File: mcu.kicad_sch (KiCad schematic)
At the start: 34 parts, among them J2 USB-C, J3 UART0, J4 I2C / Qwiic, J5 SPI, J6 WS2812, J7 Spare IO, J8 Rail break-out, SW1 RESET, SW2 BOOT, U4 ESP32-S3-WROOM-1-N16R8, U5 USBLC6-2SC6, U6 74AHCT1G125

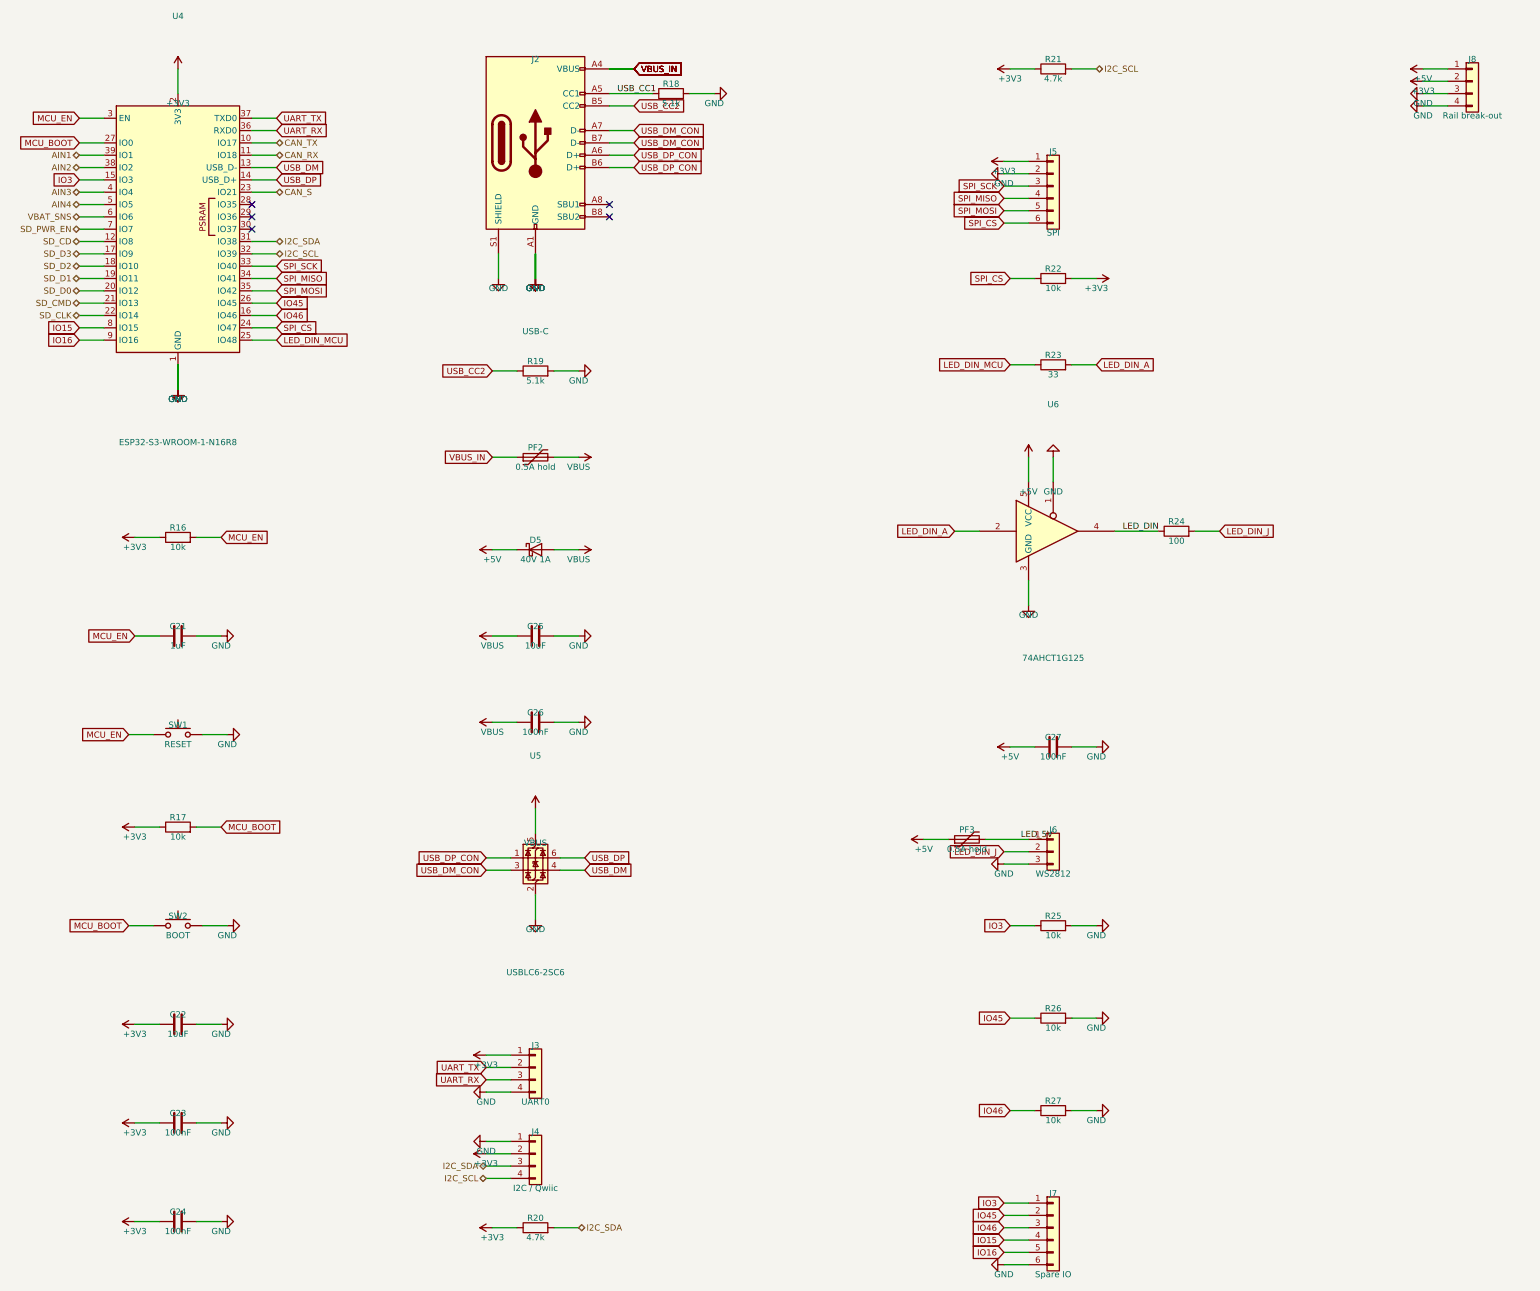
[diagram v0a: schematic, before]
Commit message: Turn the USB-C round, clamp ahead of the FET, draw the last two blocks
Two review findings from Matt, both correct:

  - The USB-C receptacle faced the wrong way. Its fab outline runs
    y -3.65..+3.65 and the signal pads sit at y -4.04, outside it: the
    contacts leave the REAR of the shell, so at 0 degrees the mouth faces
    +y, and at the 270 it was placed at the opening pointed back into the
    middle of the board. At 90 the mouth ends ~2 mm inside the right edge
    -- the plug approaches over the top of the laminate, so those last
    2 mm are not in its way -- and the pad row faces inboard, which is
    where the D+/D- via columns and the USBLC6 already were.

  - The transient clamp was behind the reverse-battery FET, which leaves
    Q1 and the LM74700 exposed to whatever arrives on the harness: on a
    negative transient Q1 turns off and stands the whole pulse across its
    drain-source, and ISO 7637-2 pulse 1 (-100V) and 3a (-150V) both
    exceed its 100V rating. It now sits on VBAT_F, straight after the
    fuse and ahead of the ferrite and the FET.

    It also changes from SMCJ40A to SMCJ40CA. A unidirectional part in
    that position forward-conducts on a sustained reverse connection and
    blows the fuse -- exactly the outcome the ideal diode exists to
    avoid. Bidirectional stands off 40V either way, so -14V reverse
    battery is still Q1's job to block and only real transients clamp.
    Needs an LCSC pick at order time, as the SMCJ40A did.

The power front end and the USB port are now hand-drawn blocks too, so
every recurring circuit on the board comes from gen/sch_blocks.py.

Board rerouted from scratch at 60 autoroute passes: 0 DRC violations,
0 unconnected. Netlist matches node for node, ERC clean. fab/ regenerated.

Co-Authored-By: Claude Opus 5 <noreply@anthropic.com>
Claude-Session: https://claude.ai/code/session_01DhNbL25h25p8VFCjRfJik9
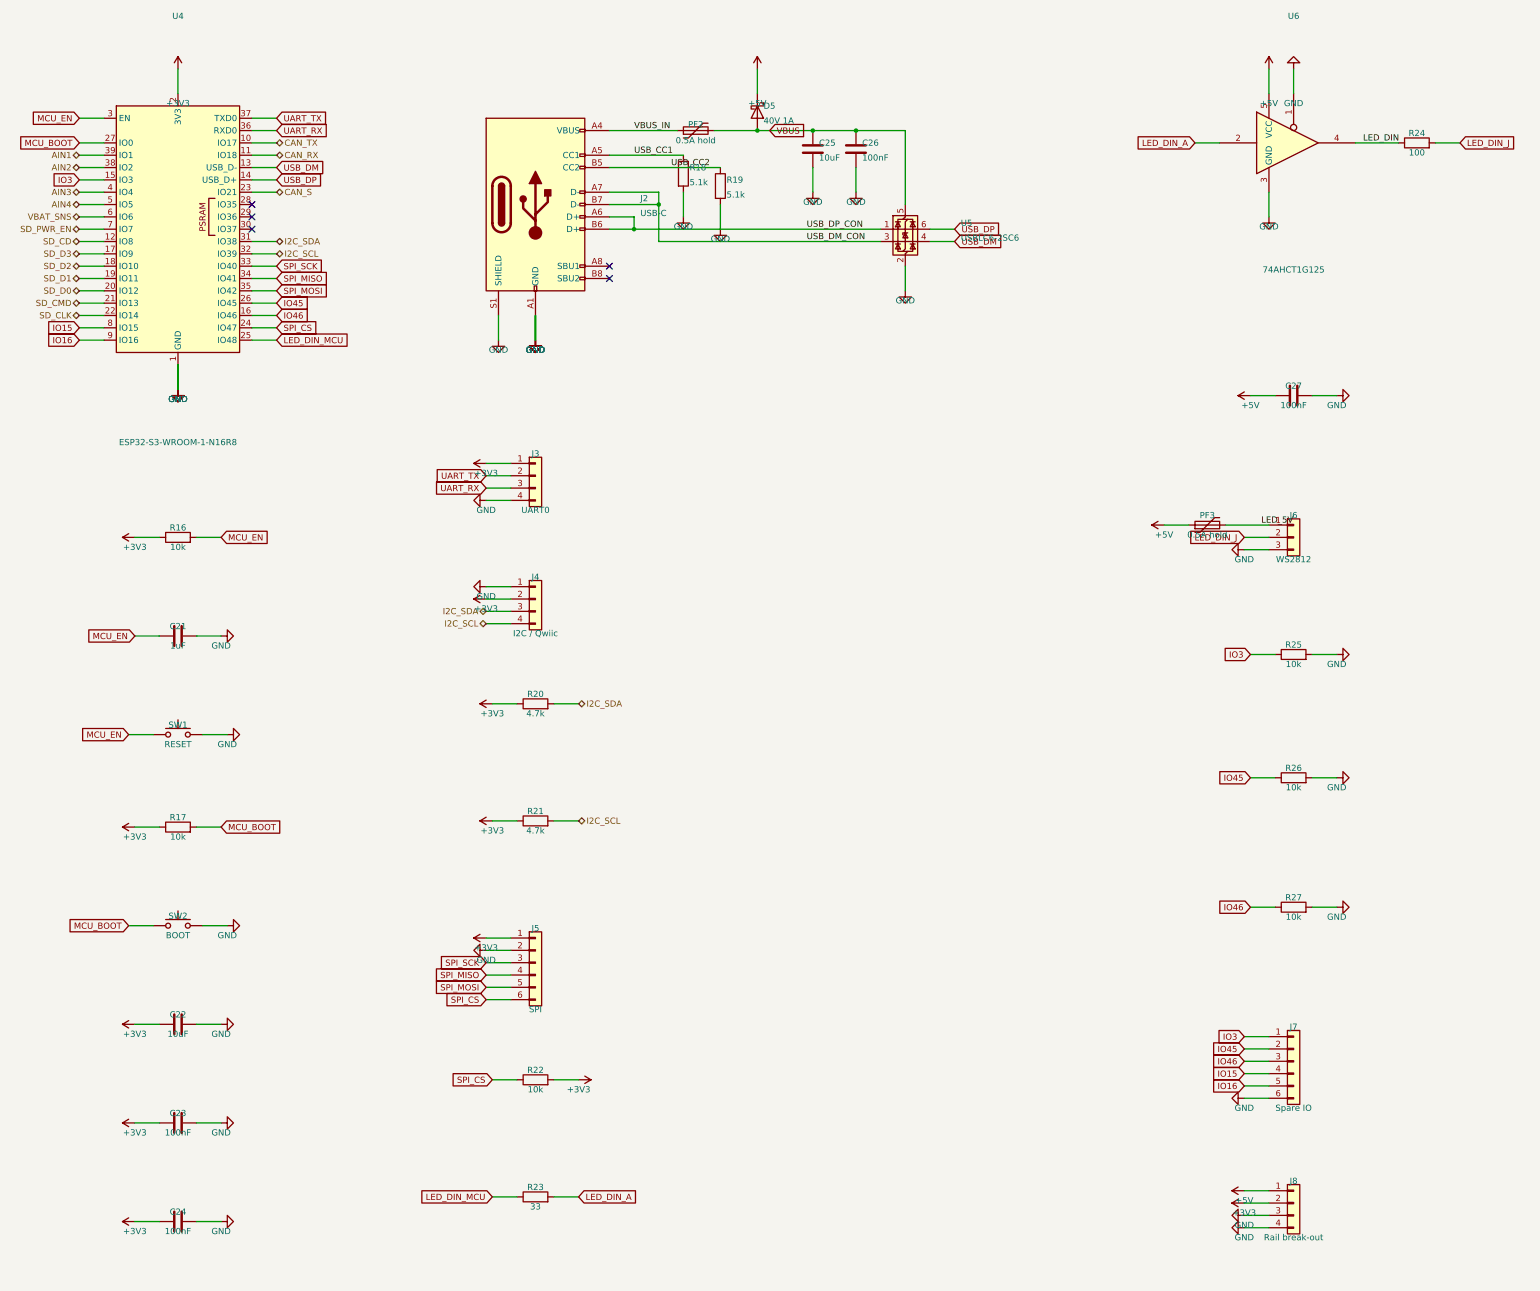
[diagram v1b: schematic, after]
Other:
- moved on the sheet: C25, C26, C27, D5, J2, J3, J4, J5, J6, J7, J8, PF2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
